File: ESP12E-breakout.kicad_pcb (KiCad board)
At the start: 2 copper layers, 27 x 35 mm, 12 parts, among them P1 CONN_01X08, P2 CONN_01X06, P3 CONN_01X08, SW1 RESET, SW2 FLASH, U1 ESP-12E

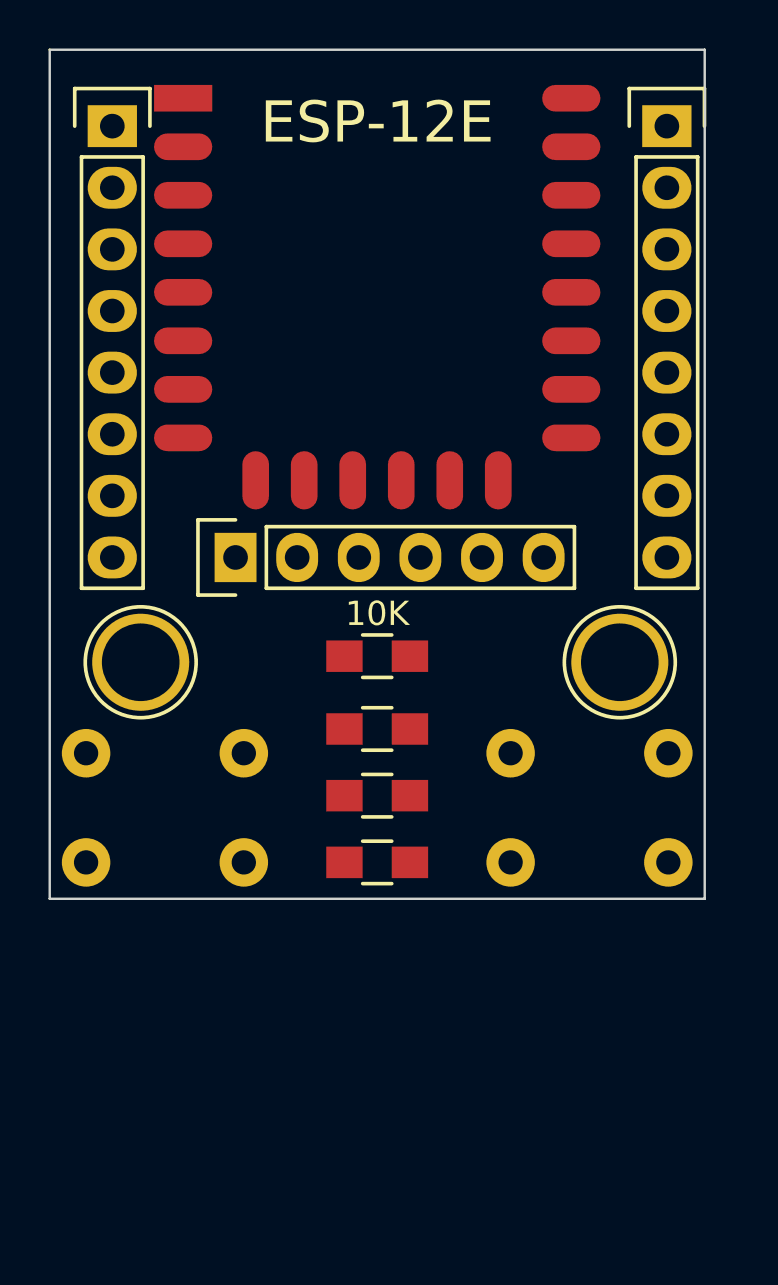
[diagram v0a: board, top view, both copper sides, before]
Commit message: Added on board bi-directional 3v3-5V conversion
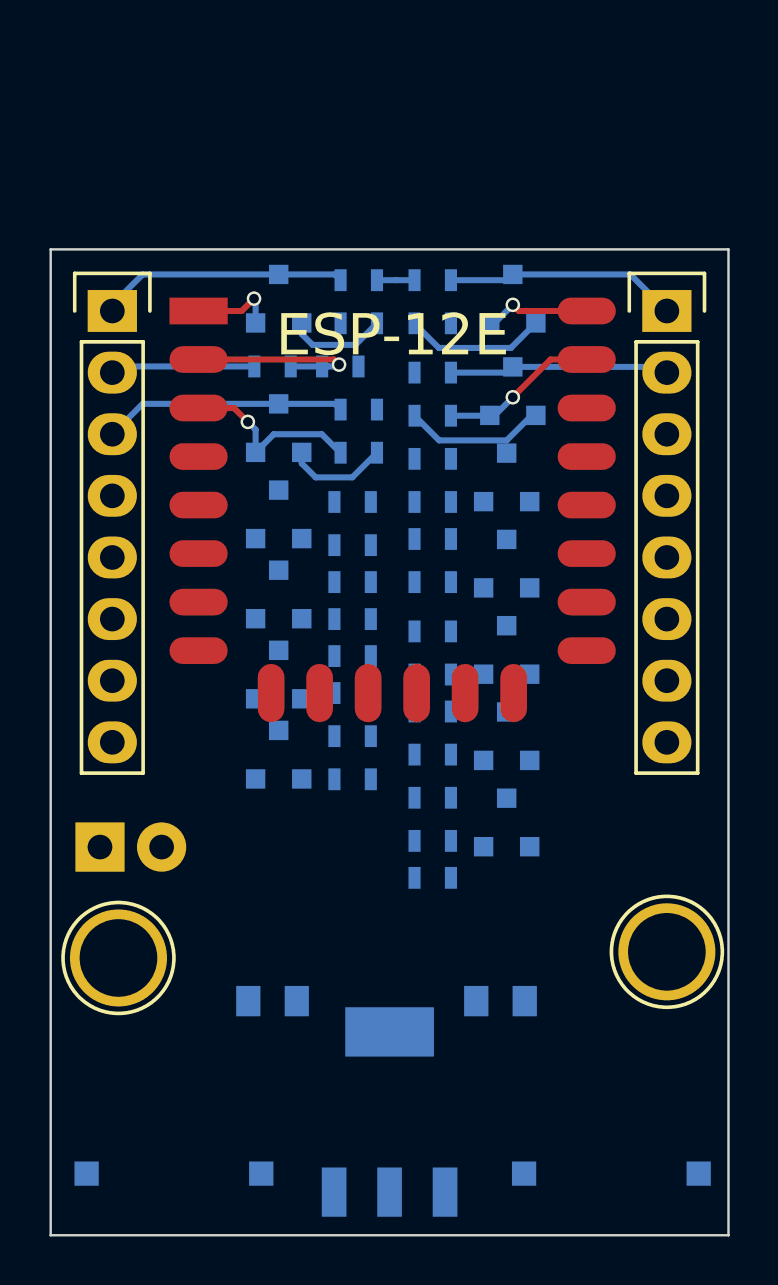
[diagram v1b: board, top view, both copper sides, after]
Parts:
- added C1: 10uF, Capacitors_SMD:C_0805, B.Cu at (138.7, 125.0)
- added C2: 100uF, Capacitors_SMD:C_0805, B.Cu at (148.1, 125.0)
- added Q1: BSS138, TO_SOT_Packages_SMD:SOT-23, B.Cu at (138.9, 96.0)
- added Q10: BSS138, TO_SOT_Packages_SMD:SOT-23, B.Cu at (148.3, 117.6)
- added Q11: BSS138, TO_SOT_Packages_SMD:SOT-23, B.Cu at (148.6, 96.0)
- added Q12: BSS138, TO_SOT_Packages_SMD:SOT-23, B.Cu at (148.6, 99.8)
- added Q13: BSS138, TO_SOT_Packages_SMD:SOT-23, B.Cu at (148.3, 103.4)
- added Q2: BSS138, TO_SOT_Packages_SMD:SOT-23, B.Cu at (138.9, 101.3)
- added Q3: BSS138, TO_SOT_Packages_SMD:SOT-23, B.Cu at (138.9, 104.9)
- added Q4: BSS138, TO_SOT_Packages_SMD:SOT-23, B.Cu at (138.9, 108.2)
- added Q5: BSS138, TO_SOT_Packages_SMD:SOT-23, B.Cu at (138.9, 111.5)
- added Q6: BSS138, TO_SOT_Packages_SMD:SOT-23, B.Cu at (138.9, 114.8)
- added Q7: BSS138, TO_SOT_Packages_SMD:SOT-23, B.Cu at (148.3, 110.5)
- added Q8: BSS138, TO_SOT_Packages_SMD:SOT-23, B.Cu at (148.3, 106.9)
- added Q9: BSS138, TO_SOT_Packages_SMD:SOT-23, B.Cu at (148.3, 114.0)
- added R10: 10K, Resistors_SMD:R_0603, B.Cu at (142.2, 100.6)
- added R11: 10K, Resistors_SMD:R_0603, B.Cu at (142.0, 104.4)
- added R12: 10K, Resistors_SMD:R_0603, B.Cu at (142.0, 107.7)
- added R13: 10K, Resistors_SMD:R_0603, B.Cu at (142.0, 110.7)
- added R14: 10K, Resistors_SMD:R_0603, B.Cu at (142.0, 114.0)
- added R15: 10K, Resistors_SMD:R_0603, B.Cu at (145.3, 119.9)
- added R16: 10K, Resistors_SMD:R_0603, B.Cu at (145.3, 111.5)
- added R17: 10K, Resistors_SMD:R_0603, B.Cu at (145.3, 107.7)
- added R18: 10K, Resistors_SMD:R_0603, B.Cu at (145.3, 114.8)
- added R19: 10K, Resistors_SMD:R_0603, B.Cu at (145.3, 118.4)
- added R20: 10K, Resistors_SMD:R_0603, B.Cu at (145.3, 97.0)
- added R21: 10K, Resistors_SMD:R_0603, B.Cu at (145.3, 100.8)
- added R22: 10K, Resistors_SMD:R_0603, B.Cu at (145.3, 104.4)
- added R23: 10K, Resistors_SMD:R_0603, B.Cu at (145.3, 109.7)
- added R24: 10K, Resistors_SMD:R_0603, B.Cu at (145.3, 105.9)
- added R25: 10K, Resistors_SMD:R_0603, B.Cu at (145.3, 113.0)
- added R26: 10K, Resistors_SMD:R_0603, B.Cu at (145.3, 116.6)
- added R27: 10K, Resistors_SMD:R_0603, B.Cu at (145.3, 95.2)
- added R28: 10K, Resistors_SMD:R_0603, B.Cu at (145.3, 99.1)
- added R29: 10K, Resistors_SMD:R_0603, B.Cu at (145.3, 102.6)
- added R5: 10K, Resistors_SMD:R_0603, B.Cu at (142.0, 112.3)
- added R6: 10K, Resistors_SMD:R_0603, B.Cu at (142.0, 115.8)
- added R7: 10K, Resistors_SMD:R_0603, B.Cu at (138.7, 98.8)
- added R8: 2.2K, Resistors_SMD:R_0603, B.Cu at (141.5, 98.8)
- added R9: 10K, Resistors_SMD:R_0603, B.Cu at (142.2, 95.2)
- added U2: AP1117, TO_SOT_Packages_SMD:SOT-223_edit, B.Cu at (143.5, 129.5)
- P1: value CONN_01X08 -> Power; footprint Pin_Headers:Pin_Header_Straight_1x08 -> Pin_Headers:Pin_Header_Straight_1x02; moved to B.Cu
- P2: value CONN_01X06 -> CONN_01X08; footprint Pin_Headers:Pin_Header_Straight_1x06 -> Pin_Headers:Pin_Header_Straight_1x08
- R1, R2, R3, R4: footprint Resistors_SMD:R_0805_HandSoldering -> Resistors_SMD:R_0603; moved to B.Cu
- SW1, SW2: footprint w_switch:PCB_PUSH_edit -> w_switch:smd_push
- moved P1 29.7 mm to (131.6, 118.6), turned to 270 degrees
- moved REF** 24.8 mm to (154.9, 122.9)
- moved REF** 24.0 mm to (132.3, 123.2)
- moved SW2 15.1 mm to (152.7, 132.1), turned to 180 degrees
- moved SW1 15.1 mm to (134.6, 132.1), turned to 0 degrees
- moved R1 13.7 mm to (142.2, 97.0), turned to 0 degrees
- moved R2 11.4 mm to (142.2, 102.4), turned to 0 degrees
- moved P2 11.4 mm to (132.1, 96.5), turned to 0 degrees
- moved R3 10.4 mm to (142.0, 106.2), turned to 0 degrees
- moved R4 10.1 mm to (142.0, 109.2)
- moved U1 8.79 mm to (135.6, 96.5)
- moved P3 7.62 mm to (154.9, 96.5)
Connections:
- P1 pad 1: Net-(P1-Pad1) -> /5V
- P1 pad 2: Net-(P1-Pad2) -> GND
- P2 pad 1: Net-(P2-Pad1) -> /RESET_HV
- P2 pad 2: Net-(P2-Pad2) -> /ADC_HV
- P2 pad 3: Net-(P2-Pad3) -> /CH_PD_HV
- P2 pad 4: Net-(P2-Pad4) -> /16_HV
- P2 pad 5: Net-(P2-Pad5) -> /14_HV
- P2 pad 6: Net-(P2-Pad6) -> /12_HV
- P3 pad 1: Net-(P3-Pad1) -> /TX_HV
- P3 pad 2: Net-(P3-Pad2) -> /RX_HV
- P3 pad 3: Net-(P3-Pad3) -> /5_HV
- P3 pad 4: Net-(P3-Pad4) -> /4_HV
- P3 pad 5: /0 -> /0_HV
- P3 pad 6: /2 -> /2_HV
- P3 pad 7: /15 -> /15_HV
- R1 pad 1: Net-(P1-Pad1) -> /RESET
- R1 pad 2: /VCC -> /3V3
- R2 pad 2: /VCC -> /3V3
- R3 pad 1: /2 -> /16
- R3 pad 2: /VCC -> /3V3
- R4 pad 1: GND -> /14
- R4 pad 2: /15 -> /3V3
- SW1 pad 1: Net-(P1-Pad1) -> GND
- SW1 pad 2: GND -> /RESET
- U1 pad 1: Net-(P1-Pad1) -> /RESET
- U1 pad 10: Net-(P2-Pad2) -> Net-(U1-Pad10)
- U1 pad 11: Net-(P2-Pad3) -> Net-(U1-Pad11)
- U1 pad 12: Net-(P2-Pad4) -> Net-(U1-Pad12)
- U1 pad 13: Net-(P2-Pad5) -> Net-(U1-Pad13)
- U1 pad 14: Net-(P2-Pad6) -> Net-(U1-Pad14)
- U1 pad 19: Net-(P3-Pad4) -> /4
- U1 pad 2: Net-(P1-Pad2) -> /ADC
- U1 pad 20: Net-(P3-Pad3) -> /5
- U1 pad 21: Net-(P3-Pad2) -> /RX
- U1 pad 22: Net-(P3-Pad1) -> /TX
- U1 pad 4: Net-(P1-Pad4) -> /16
- U1 pad 5: Net-(P1-Pad5) -> /14
- U1 pad 6: Net-(P1-Pad6) -> /12
- U1 pad 7: Net-(P1-Pad7) -> /13
- U1 pad 8: /VCC -> /3V3
- U1 pad 9: Net-(P2-Pad1) -> Net-(U1-Pad9)
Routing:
- net /3V3: track 0.00 -> 20.1 mm
- net /RESET_HV: track 0.00 -> 10.3 mm
- net /CH_PD_HV: track 0.00 -> 10.0 mm
- net /TX_HV: track 0.00 -> 9.62 mm
- net /RX_HV: track 0.00 -> 9.10 mm
- net /ADC: track 0.00 -> 8.14 mm, vias 0 -> 1
- net /CH_PD: track 0.00 -> 7.78 mm, vias 0 -> 1
- net /RX: track 0.00 -> 6.56 mm, vias 0 -> 1
- net /ADC_HV: track 0.00 -> 5.96 mm
- net /TX: track 0.00 -> 4.41 mm, vias 0 -> 1
- net /RESET: track 0.00 -> 3.52 mm, vias 0 -> 1
- net /5V: track 0.00 -> 1.57 mm
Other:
- board size 27 x 35 mm -> 27.9 x 40.6 mm
- board text added: "(CK)14"
- board text added: "(SI)13"
- board text added: "(SO)12"
- board text added: "4(SD)"
- board text added: "5(SC)"
- board text added: "~R"
- board text removed: "(MISO)12"
- board text removed: "(MOSI)13"
- board text removed: "(SCK)14"
- board text removed: "4(SDA)"
- board text removed: "5(SCL)"
- board text removed: "MTCK"
- board text removed: "MTDI"
- board text removed: "MTDO"
- board text removed: "MTMS"
- board text removed: "RESET"
- board text removed: "SD_2"
- board text removed: "SD_3"

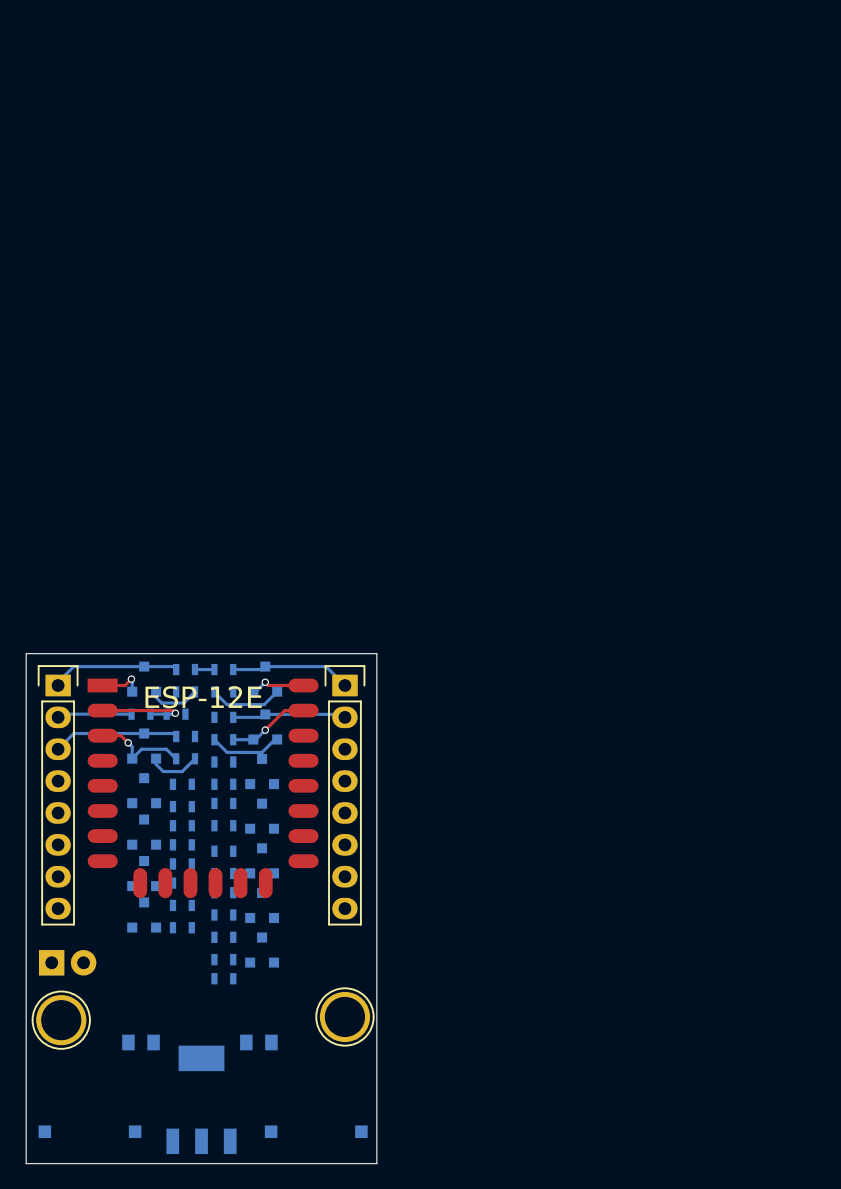
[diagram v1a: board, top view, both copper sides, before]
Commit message: Keeping it simple Removed the level conversion, added regulator and other pull ups and pull donws.
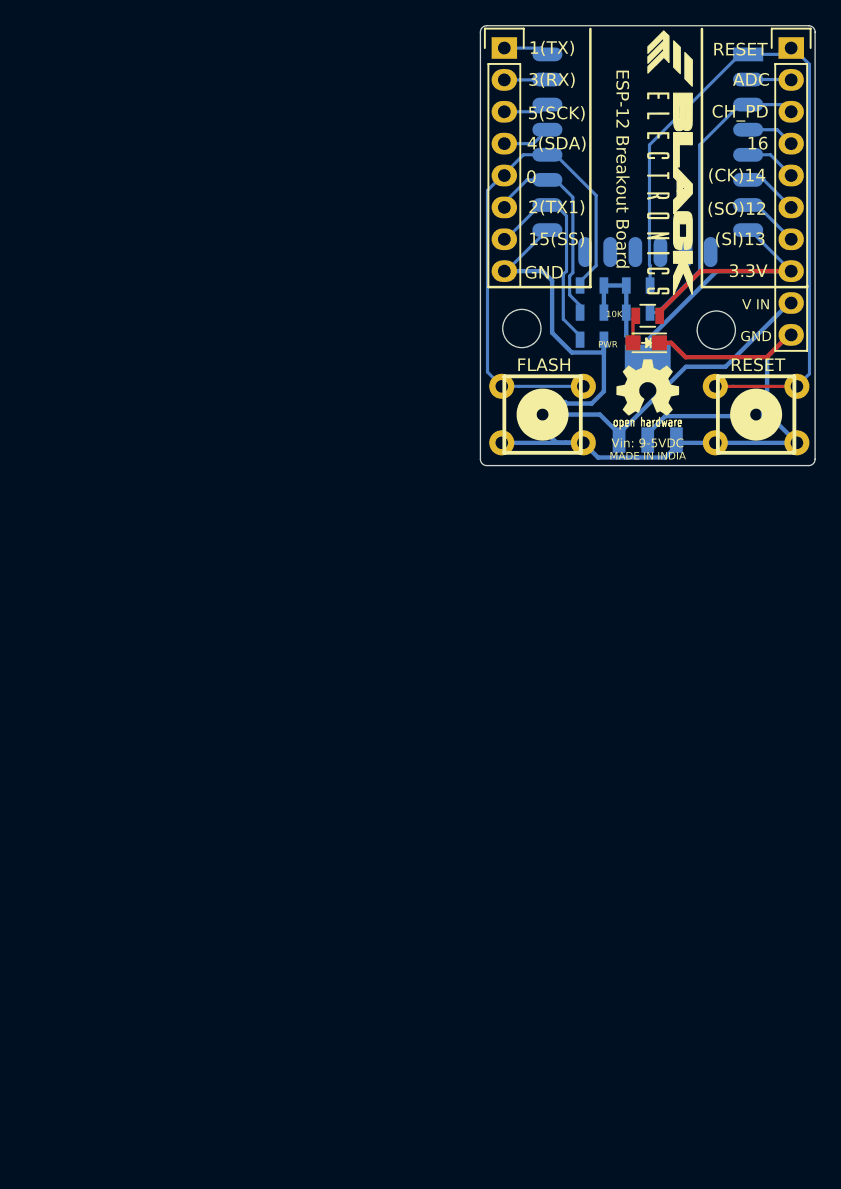
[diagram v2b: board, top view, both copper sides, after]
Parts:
- removed P2: CONN_01X08, Pin_Headers:Pin_Header_Straight_1x08
- removed Q1, Q10, Q11, Q12, Q13, Q2, Q3, Q4, Q5, Q6, Q7, Q8, Q9: BSS138, TO_SOT_Packages_SMD:SOT-23
- removed R10, R11, R12, R13, R14, R15, R16, R17, R18, R19, R20, R21, R22, R23, R24, R25, R26, R27, R28, R29, R7, R9: 10K, Resistors_SMD:R_0603
- removed R8: 2.2K, Resistors_SMD:R_0603
- removed REF** (x2): 1pin, Connect:1pin
- added D1: PWR, LEDs:LED-0805, F.Cu at (178.9, 69.2)
- added G***: LOGO, logo:3k5, F.Cu at (180.8, 54.9)
- added G***: LOGO, logo:oshw-logo-kicad-copper-10mm, F.Cu at (179.1, 72.8)
- P1: value Power -> CONN_01X10; footprint Pin_Headers:Pin_Header_Straight_1x02 -> Pin_Headers:Pin_Header_Straight_1x10; moved to F.Cu
- R1, R2, R3, R4, R5: footprint Resistors_SMD:R_0603 -> Resistors_SMD:R_0805
- R6: footprint Resistors_SMD:R_0603 -> Resistors_SMD:R_0805; moved to F.Cu
- SW1, SW2: footprint w_switch:smd_push -> w_switch:PCB_PUSH_edit; moved to F.Cu
- U1: moved to B.Cu
- moved P1 93.7 mm to (190.5, 45.7), turned to 0 degrees
- moved SW1 78.0 mm to (187.7, 74.9), turned to 90 degrees
- moved U1 71.9 mm to (187.1, 46.2), turned to 180 degrees
- moved U2 66.2 mm to (179.1, 73.7)
- moved C2 63.6 mm to (187.6, 75.1)
- moved R6 61.3 mm to (179.1, 67.1)
- moved SW2 59.9 mm to (170.7, 74.9), turned to 270 degrees
- moved C1 59.4 mm to (170.7, 74.9), turned to 180 degrees
- moved R5 54.2 mm to (174.6, 69.0), turned to 180 degrees
- moved R4 53.5 mm to (174.6, 66.8)
- moved R3 52.8 mm to (174.6, 64.6)
- moved P3 52.4 mm to (167.6, 45.7)
- moved R2 50.6 mm to (178.3, 66.8), turned to 180 degrees
- moved R1 48.5 mm to (178.3, 64.6), turned to 180 degrees
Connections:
- P1 pad 1: /5V -> /RESET
- P1 pad 2: GND -> /ADC
- P3 pad 1: /TX_HV -> /TX
- P3 pad 2: /RX_HV -> /RX
- P3 pad 3: /5_HV -> /5
- P3 pad 4: /4_HV -> /4
- P3 pad 5: /0_HV -> /0
- P3 pad 6: /2_HV -> /2
- P3 pad 7: /15_HV -> /15
- R3 pad 1: /16 -> /0
- R4 pad 1: /14 -> /2
- R5 pad 1: /12 -> GND
- R5 pad 2: /3V3 -> /15
- R6 pad 1: /13 -> Net-(D1-Pad2)
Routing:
- net GND: track 0.00 -> 82.4 mm
- net /RESET: track 3.52 -> 60.3 mm, vias 1 -> 0
- net /0: track 0.00 -> 41.5 mm
- net /3V3: track 20.1 -> 50.9 mm
- net /5V: track 1.57 -> 24.3 mm
- net /15: track 0.00 -> 17.0 mm
- net /2: track 0.00 -> 16.8 mm
- net /CH_PD: track 7.78 -> 24.2 mm, vias 1 -> 0
- net /RESET_HV: track 10.3 -> 0.00 mm
- net /CH_PD_HV: track 10.0 -> 0.00 mm
- net /TX_HV: track 9.62 -> 0.00 mm
- net /RX_HV: track 9.10 -> 0.00 mm
- net /ADC_HV: track 5.96 -> 0.00 mm
- net /ADC: track 8.14 -> 3.44 mm, vias 1 -> 0
- net /13: track 0.00 -> 4.56 mm
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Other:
- board size 27.9 x 40.6 mm -> 26.7 x 35.1 mm
- net class Power added: clearance 0.2, trace_width 0.35, via_dia 0.6, via_drill 0.4
- board text added: "3.3V"
- board text added: "4(SDA)"
- board text added: "5(SCK)"
- board text added: "ESP-12 Breakout Board"
- board text added: "ETOK and Code area Bottom layer"
- board text added: "MADE IN INDIA"
- board text added: "RESET"
- board text added: "These pretzels are making me thirsty"
- board text added: "V IN"
- board text added: "Vin: 9-5VDC"
- board text removed: "4(SD)"
- board text removed: "5(SC)"
- board text removed: "VCC"
- board text removed: "~R"
